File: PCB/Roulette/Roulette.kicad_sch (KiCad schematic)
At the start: 266 parts, among them J1 USB-PROG, J2 Shelly, J3 Conn_01x03, J4 Conn_01x02, Q1 PMF170XP,115, SW1 SW_Push, U2 ESP32-S3-MINI-1

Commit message: Library update
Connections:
- net VCC renamed VLED
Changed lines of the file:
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@@
   (junction (at 35.56 139.065) (diameter 0) (color 0 0 0 0)
   )
-  (junction (at 8.89 24.765) (diameter 0) (color 0 0 0 0)
-  )
   (junction (at 290.83 55.88) (diameter 0) (color 0 0 0 0)
   )
@@
   (junction (at 31.75 94.615) (diameter 0) (color 0 0 0 0)
   )
+  (junction (at 8.89 24.765) (diameter 0) (color 0 0 0 0)
+  )
   (junction (at 208.915 53.975) (diameter 0) (color 0 0 0 0)
   )
@@
     (stroke (width 0) (type default))
   )
-  (wire (pts (xy 8.89 20.955) (xy 8.89 24.765))
-    (stroke (width 0) (type default))
-  )
   (wire (pts (xy 58.42 31.115) (xy 58.42 37.465))
     (stroke (width 0) (type default))
@@
     (stroke (width 0) (type default))
   )
+  (wire (pts (xy 8.89 20.955) (xy 8.89 24.765))
+    (stroke (width 0) (type default))
+  )
   (wire (pts (xy 145.415 76.835) (xy 146.05 76.835))
     (stroke (width 0) (type default))
@@
         )
       )
-    )
-  )
-  (symbol (lib_id "power:VCC") (at 8.89 24.765 0) (unit 1)
-    (in_bom yes) (on_board yes) (dnp no) (fields_autoplaced)
-    (property "Reference" "#PWR03" (at 8.89 28.575 0)
-      (effects (font (size 1.27 1.27)) hide)
-    )
-    (property "Value" "VCC" (at 8.89 20.6319 0)
-      (effects (font (size 1.27 1.27)))
-    )
-    (property "Footprint" "" (at 8.89 24.765 0)
-      (effects (font (size 1.27 1.27)) hide)
-    )
-    (property "Datasheet" "" (at 8.89 24.765 0)
-      (effects (font (size 1.27 1.27)) hide)
-    )
-    (pin "1")
-    (instances
-      (project "Roulette"
-        (path "/46c350bb-7de4-4e81-aafd-4af55e37aab0"
-          (reference "#PWR03") (unit 1)
-        )
-      )

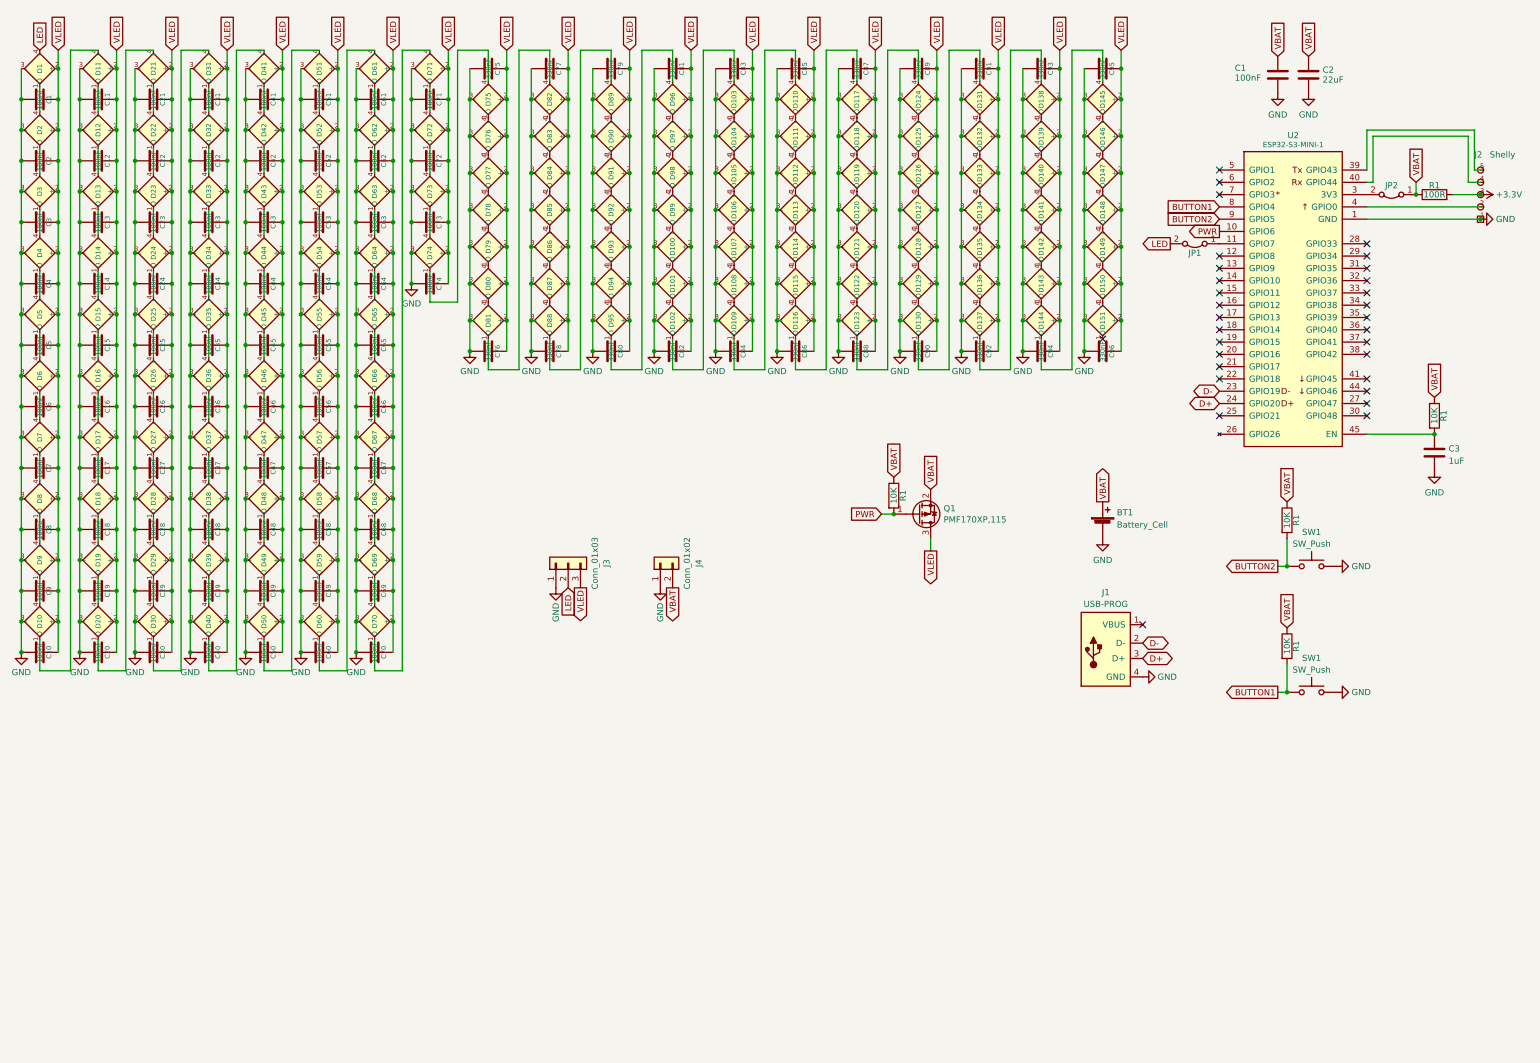
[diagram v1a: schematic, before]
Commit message: Started new h/w - needs parts and tracking
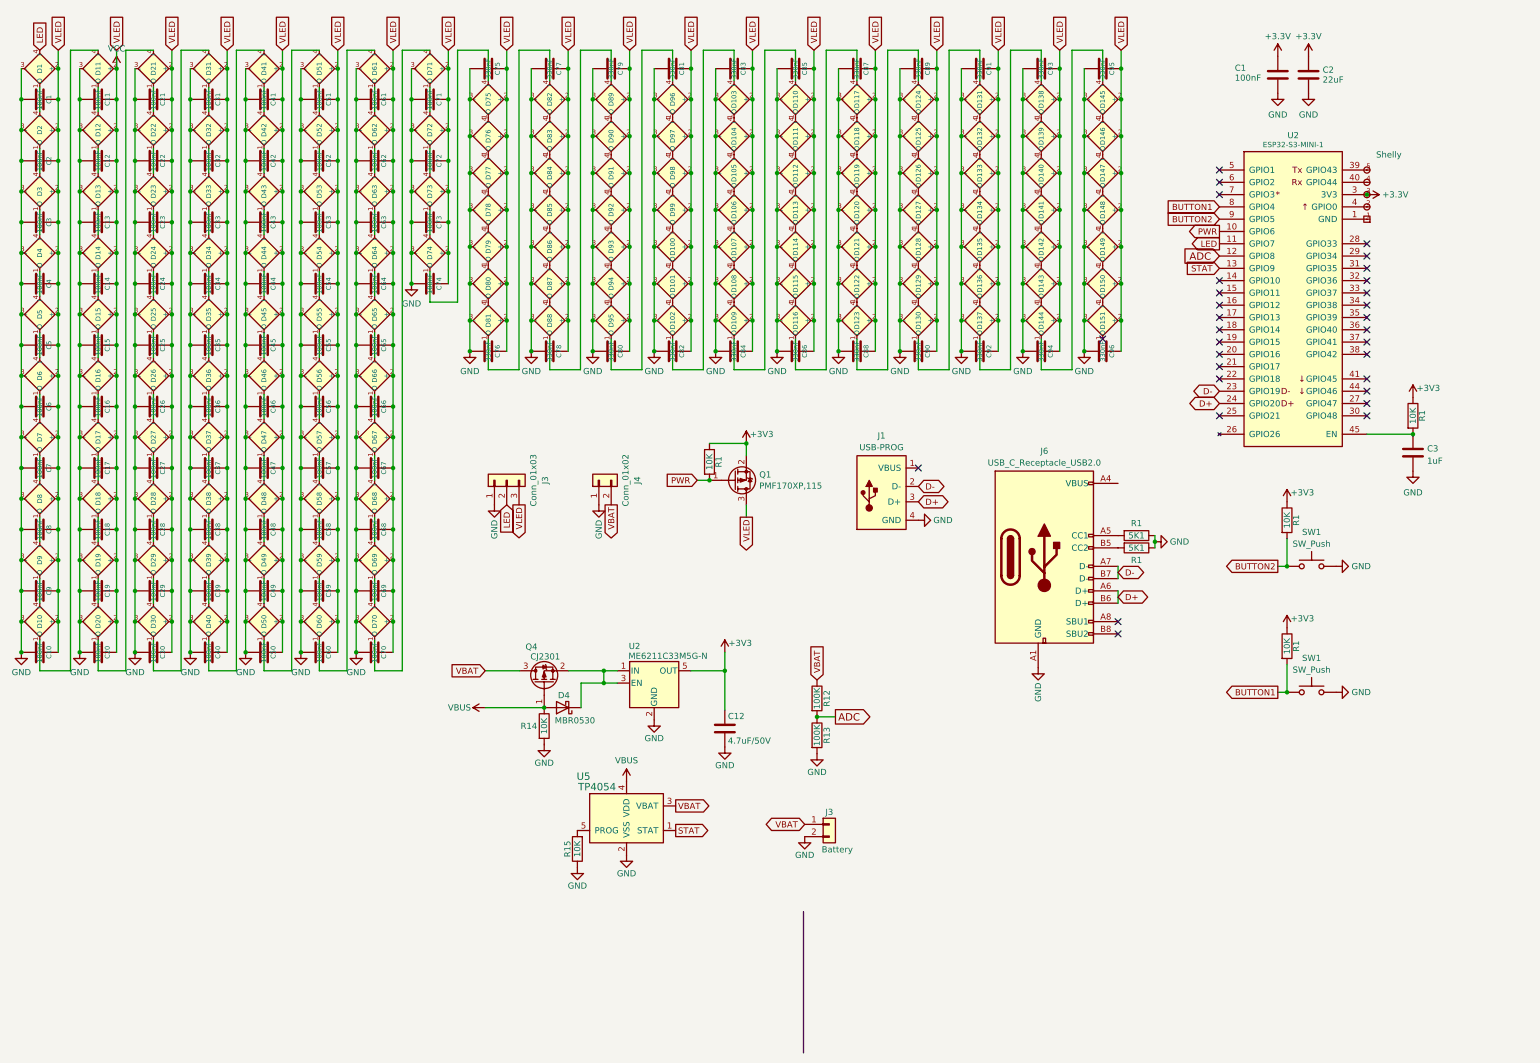
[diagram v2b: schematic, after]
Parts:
- removed BT1: Battery_Cell, RevK:Battery-Holder-2032, symbol Device:Battery_Cell
- removed JP1, JP2: Jumper_2_Bridged, RevK:Pad_1206_0805_Bridged, symbol Jumper:Jumper_2_Bridged
- removed R1: 100R, RevK:R_0402, symbol Device:R
- added C12: 4.7uF/50V, RevK:C_0805, symbol Device:C
- added D4: MBR0530, RevK:D_SOD-123, symbol Device:D_Schottky
- added J3: Battery, Connector_Molex:Molex_PicoBlade_53261-0271_1x02-1MP_P1.25mm_Horizontal, symbol Connector_Generic:Conn_01x02
- added J6: USB_C_Receptacle_USB2.0, RevK:USB_C_G_Switch-7082C, symbol RevK:USB_C_Receptacle_G_Switch_7082C
- added Q4: CJ2301, RevK:SOT-23, symbol Transistor_FET:BSS83P
- added R1 (x2): 5K1, RevK:R_0402, symbol Device:R
- added R12, R13: 100K, RevK:R_0402, symbol Device:R
- added R14, R15: 10K, RevK:R_0402, symbol Device:R
- added U2: ME6211C33M5G-N, RevK:SOT-23-5, symbol Regulator_Linear:TLV70033_SOT23-5
- added U5: TP4054, RevK:SOT-23-5, symbol Watchy-rescue:MCP73831-2-OT-Battery_Management
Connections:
- net +3V3: now also C1.1, C2.1, Q1.2 (S), R1.1, R1.1, R1.1, R1.1, U2.3 (3V3), C12.1, U2.5 (OUT)
- net D+: now also J6.A6 (D+), J6.B6 (D+)
- net D-: now also J6.A7 (D-), J6.B7 (D-)
- net GND: now also C12.2, J3.2 (Pin_2), J6.A1 (GND), R1.1, R1.1, R13.2, R14.2, R15.1, U2.2 (GND), U5.2 (VSS)
- net LED: now also U2.11 (GPIO7)
- net VBAT: now also J3.1 (Pin_1), Q4.3 (D), R12.1, U5.3 (VBAT); no longer C1.1, C2.1, Q1.2 (S), R1.1, R1.1, R1.1, R1.1
- net ADC: now reaches U2.12 (GPIO8)
- net ADC: now also R12.2, R13.1
- net STAT: now reaches U2.13 (GPIO9)
- net STAT: now also U5.1 (STAT)
- net VLED renamed VCC
- new net: D4.1 (K), Q4.2 (S), U2.1 (IN), U2.3 (EN)
- new net: J6.B5 (CC2), R1.2
- new net: J6.A5 (CC1), R1.2
- new net: R15.2, U5.5 (PROG)
- new net VBUS: D4.2 (A), Q4.1 (G), R14.1, U5.4 (VDD)
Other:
- moved on the sheet: C3, J1, J3, J4, Q1, R1

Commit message: Fix parts
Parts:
- J3: value Battery -> 53261-0271; LCSC Part # (none) -> C189700
- J6: value USB_C_Receptacle_USB2.0 -> GT-USB-7082C; LCSC Part # C3001291 -> C3001289
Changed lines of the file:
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@@
       (effects (font (size 1.27 1.27)))
     )
-    (property "Value" "Battery" (at 157.861 186.182 0)
+    (property "Value" "53261-0271" (at 157.861 186.182 0)
       (effects (font (size 1.27 1.27)))
     )
@@
     )
     (property "Datasheet" "" (at 156.21 180.975 0)
+      (effects (font (size 1.27 1.27)) hide)
+    )
+    (property "LCSC Part #" "C189700" (at 156.21 180.975 0)
       (effects (font (size 1.27 1.27)) hide)
     )
@@
       (effects (font (size 1.27 1.27)))
     )
-    (property "Value" "USB_C_Receptacle_USB2.0" (at 200.66 106.2299 0)
+    (property "Value" "GT-USB-7082C" (at 200.66 106.2299 0)
       (effects (font (size 1.27 1.27)))
     )
@@
       (effects (font (size 1.27 1.27)) hide)
     )
-    (property "LCSC Part #" "C3001291" (at 200.66 125.73 0)
-      (effects (font (size 1.27 1.27)) hide)
-    )
+    (property "LCSC Part #" "C3001289" (at 200.66 125.73 0)
+      (effects (font (size 1.27 1.27)) hide)
+    )

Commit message: Rechargable board
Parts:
- added Q1: PMF170XP,115, RevK:SOT-323_SC-70, symbol Device:Q_PMOS_GSD
- added R1: 10K, RevK:R_0402, symbol Device:R
- J3: value 53261-0271 -> JST-PH-SM3-TBT; footprint Connector_Molex:Molex_PicoBlade_53261-0271_1x02-1MP_P1.25mm_Horizontal -> Connector_JST:JST_PH_B2B-PH-SM4-TB_1x02-1MP_P2.00mm_Vertical; LCSC Part # C189700 -> C265003
- J6: LCSC Part # C3001289 -> C3001291
- Q4: LCSC Part # (none) -> C5224170
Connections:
- net ADC: now also U2.18 (GPIO14); no longer U2.12 (GPIO8)
- net BUTTON1: now also U2.11 (GPIO7); no longer U2.8 (GPIO4)
- net BUTTON2: now also U2.38 (GPIO42); no longer U2.9 (GPIO5)
- net GND: now also J3.1 (Pin_1), J6.A12 (GND), J6.B1 (GND), J6.B12 (GND), U2.5 (GPIO1), U2.6 (GPIO2); no longer J3.2 (Pin_2)
- net LED: now also U2.9 (GPIO5); no longer U2.11 (GPIO7)
- net PWR: now also U2.8 (GPIO4); no longer U2.10 (GPIO6)
- net STAT: now also U2.15 (GPIO11); no longer U2.13 (GPIO9)
- net VBAT: now also J3.2 (Pin_2), Q1.2 (S), R1.1; no longer J3.1 (Pin_1), R12.1
- net VBUS: now also J6.A4 (VBUS), J6.A9 (VBUS), J6.B4 (VBUS), J6.B9 (VBUS)
- net ADCFET: now reaches U2.19 (GPIO15)
- net ADCFET: now also Q1.1 (G), R1.2
- new net: Q1.3 (D), R12.1
- no-connect marks 31 -> 28
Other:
- moved on the sheet: R12, R13

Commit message: Part
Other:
- note added: "B08HJ53Q3C"
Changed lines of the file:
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@@
     (stroke (width 0) (type default))
+  )
+  (text "B08HJ53Q3C" (at 150.495 189.865 0)
+    (effects (font (size 1.27 1.27)) (justify left bottom))
   )
   (global_label "VLED" (shape input) (at 20.32 20.955 90) (fields_autoplaced)

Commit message: Ordered
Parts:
- J6: value GT-USB-7082C -> C3001289; footprint RevK:USB_C_G_Switch-7082C -> RevK:USB_C_G_Switch-7082A; LCSC Part # C3001291 -> C3001289
- Q1: value PMF170XP,115 -> C179347; LCSC Part # (none) -> C179347
- Q4, U5: JLCPCB Rotation Offset (none) -> 180
- U2: JLCPCB Rotation Offset (none) -> -90
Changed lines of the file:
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@@
       (effects (font (size 1.27 1.27)) hide)
     )
+    (property "JLCPCB Rotation Offset" "-90" (at 120.015 151.765 0)
+      (effects (font (size 1.27 1.27)) hide)
+    )
     (pin "1")
     (pin "2")
@@
       (effects (font (size 1.27 1.27)) (justify left))
     )
-    (property "Value" "PMF170XP,115" (at 141.732 110.998 0)
+    (property "Value" "C179347" (at 141.732 110.998 0)
       (effects (font (size 1.27 1.27)) (justify left))
     )
@@
       (effects (font (size 1.27 1.27)) hide)
     )
+    (property "LCSC Part #" "C179347" (at 136.525 109.855 0)
+      (effects (font (size 1.27 1.27)) hide)
+    )
     (pin "1")
     (pin "2")
@@
       (effects (font (size 1.27 1.27)))
     )
-    (property "Value" "GT-USB-7082C" (at 200.66 106.2299 0)
+    (property "Value" "C3001289" (at 200.66 106.2299 0)
       (effects (font (size 1.27 1.27)))
     )
-    (property "Footprint" "RevK:USB_C_G_Switch-7082C" (at 204.47 125.73 0)
+    (property "Footprint" "RevK:USB_C_G_Switch-7082A" (at 204.47 125.73 0)
       (effects (font (size 1.27 1.27)) hide)
     )
@@
       (effects (font (size 1.27 1.27)) hide)
     )
-    (property "LCSC Part #" "C3001291" (at 200.66 125.73 0)
+    (property "LCSC Part #" "C3001289" (at 200.66 125.73 0)
       (effects (font (size 1.27 1.27)) hide)
     )
@@
       (effects (font (size 1.27 1.27)) (justify left))
     )
-    (property "Value" "PMF170XP,115" (at 164.592 138.303 0)
+    (property "Value" "C179347" (at 164.592 138.303 0)
       (effects (font (size 1.27 1.27)) (justify left))
     )
@@
       (effects (font (size 1.27 1.27)) hide)
     )
+    (property "LCSC Part #" "C179347" (at 159.385 137.16 0)
+      (effects (font (size 1.27 1.27)) hide)
+    )
     (pin "1")
     (pin "2")
@@
       (effects (font (size 1.27 1.27)) hide)
     )
+    (property "JLCPCB Rotation Offset" "180" (at 114.3 179.705 0)
+      (effects (font (size 1.27 1.27)) hide)
+    )
     (pin "1")
     (pin "2")
@@
       (effects (font (size 1.27 1.27)) hide)
     )
+    (property "JLCPCB Rotation Offset" "180" (at 97.282 151.765 90)
+      (effects (font (size 1.27 1.27)) hide)
+    )

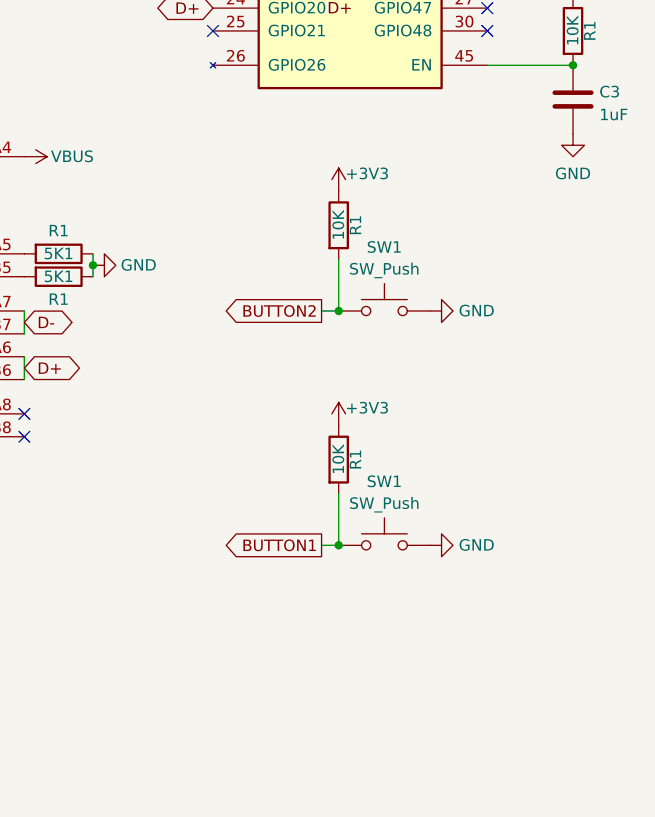
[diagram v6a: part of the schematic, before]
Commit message: Buttons active high for ext1 login in ESP
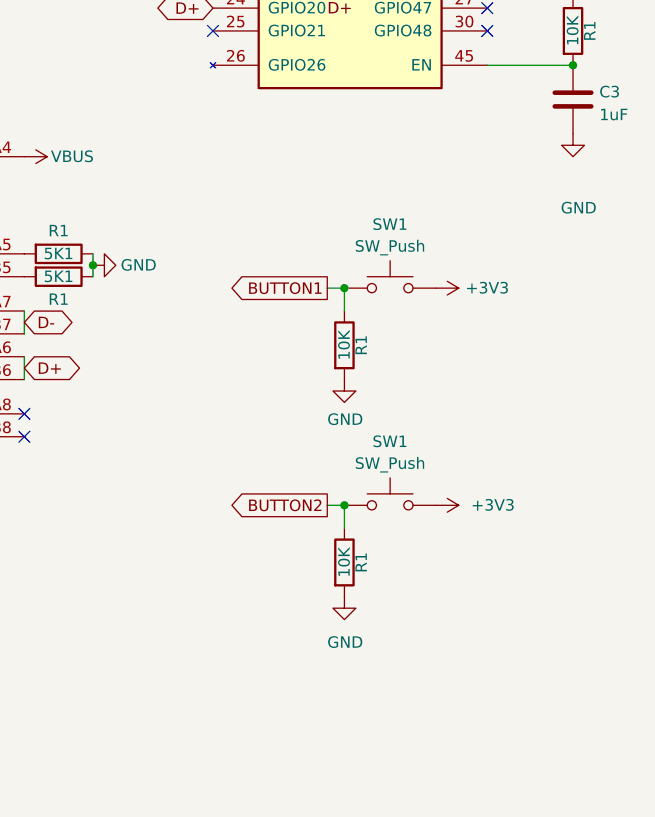
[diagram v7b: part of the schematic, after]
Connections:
- net +3V3: now also SW1.2, SW1.2; no longer R1.1, R1.1
- net BUTTON1: now also R1.1, SW1.1; no longer R1.2, SW1.1
- net BUTTON2: now also R1.1, SW1.1; no longer R1.2, SW1.1
- net GND: now also R1.2, R1.2; no longer SW1.2, SW1.2
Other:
- moved on the sheet: R1, SW1

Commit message: Tidy
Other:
- note removed: "B08HJ53Q3C"
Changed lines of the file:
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@@
     (stroke (width 0) (type default))
   )
-  (polyline (pts (xy 150.876 199.009) (xy 150.876 228.219))
-    (stroke (width 0) (type default))
-  )
   (wire (pts (xy 5.08 79.375) (xy 5.08 84.455))
     (stroke (width 0) (type default))
@@
     (stroke (width 0) (type default))
   )
-  (text "B08HJ53Q3C" (at 150.495 189.865 0)
-    (effects (font (size 1.27 1.27)) (justify left bottom))
-  )
   (global_label "VLED" (shape input) (at 20.32 20.955 90) (fields_autoplaced)
     (effects (font (size 1.27 1.27)) (justify left))
@@
   (symbol (lib_id "RevK:USB_C_Receptacle_G_Switch_7082C") (at 200.66 125.73 0) (unit 1)
     (in_bom yes) (on_board yes) (dnp no) (fields_autoplaced)
-    (property "Reference" "J6" (at 200.66 103.8057 0)
+    (property "Reference" "J6" (at 200.66 106.2299 0)
       (effects (font (size 1.27 1.27)))
     )
     (property "Value" "C3001289" (at 200.66 106.2299 0)
-      (effects (font (size 1.27 1.27)))
+      (effects (font (size 1.27 1.27)) hide)
     )
     (property "Footprint" "RevK:USB_C_G_Switch-7082A" (at 204.47 125.73 0)
